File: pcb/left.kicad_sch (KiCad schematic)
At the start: 59 parts, among them J10 Conn_01x15_Pin, J11 Conn_ARM_SWD_TagConnect_TC203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, J12 Conn_01x02_Socket, J7 Conn_01x15_Pin, J8 USB_C_Receptacle_USB2.0_16P, J9 Conn_01x15_Pin, Q2 IRLML6402, SW19 SW_Push, SW21 SW_Push, SW22 MX_SW_HS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

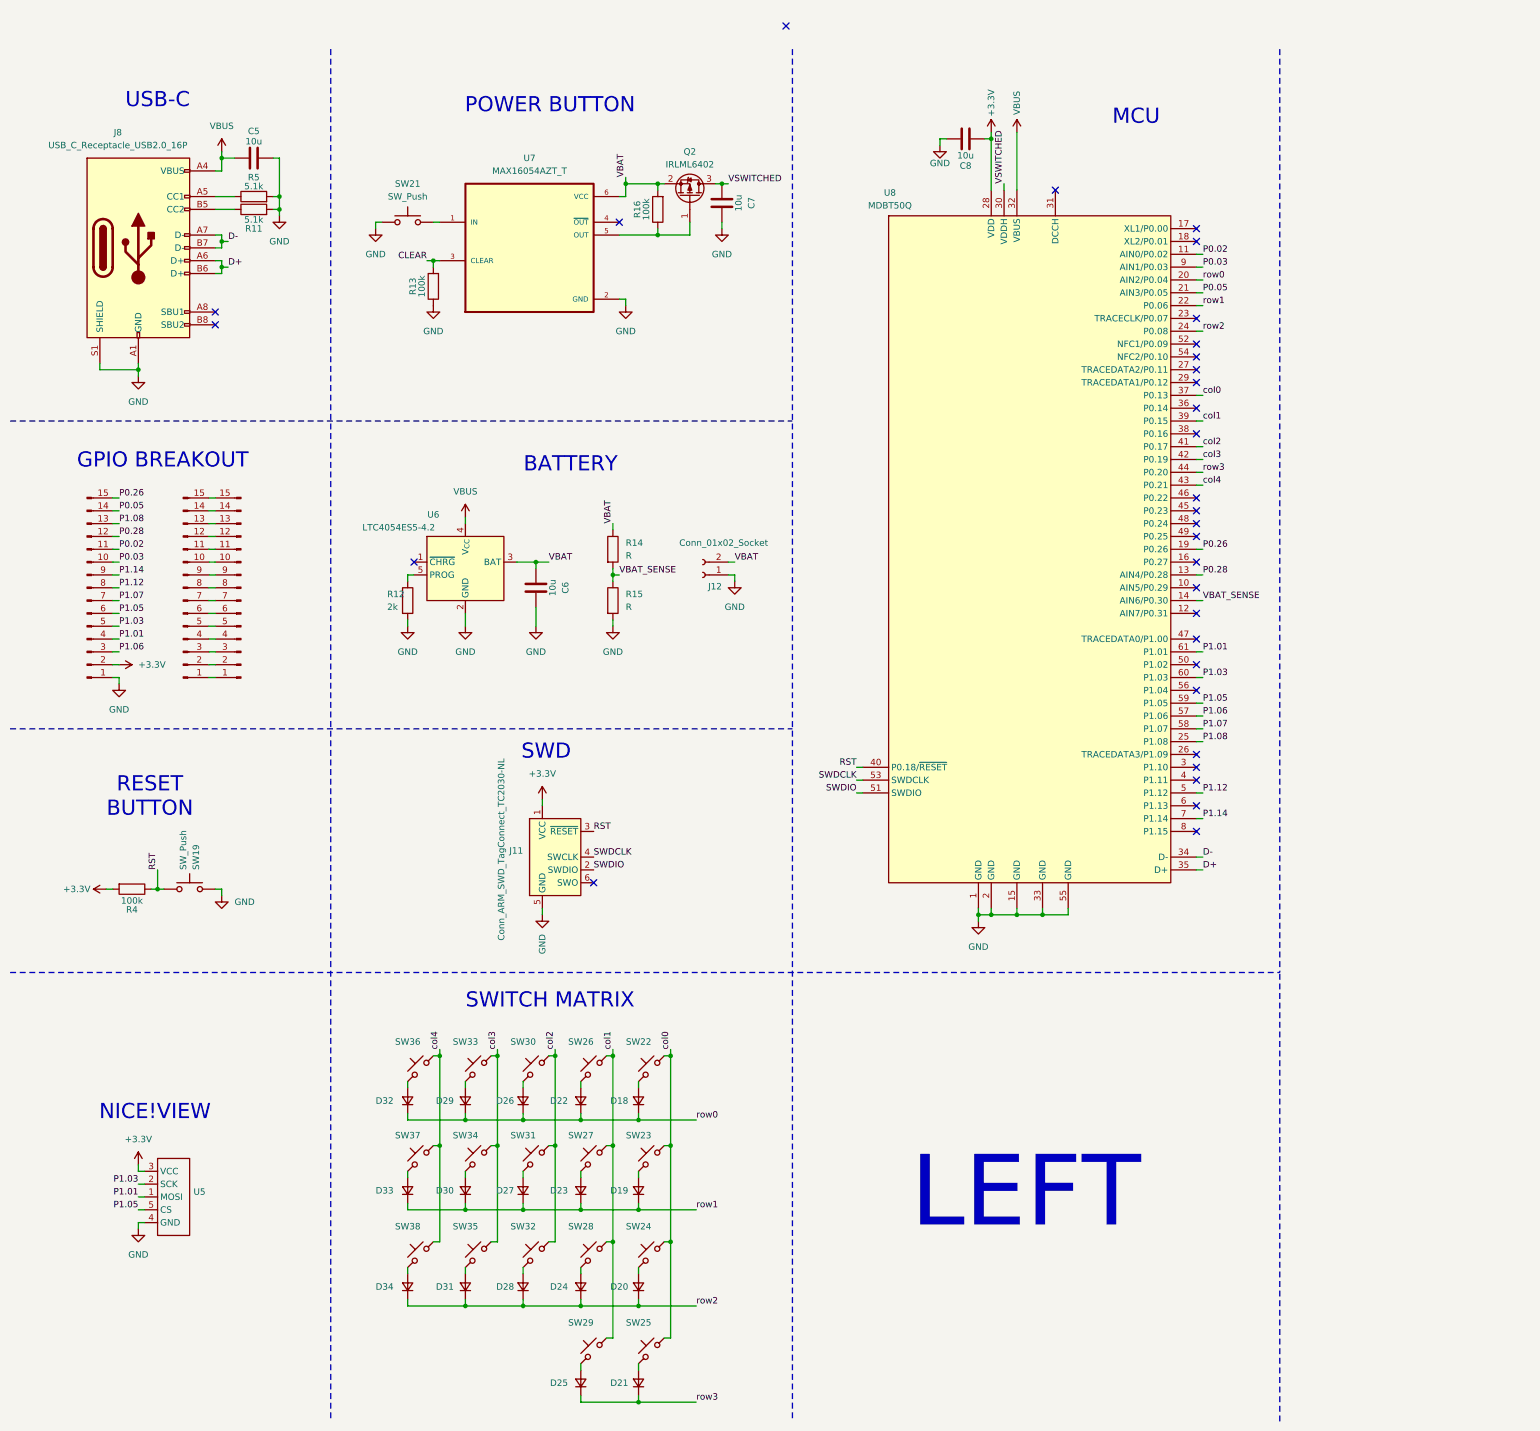
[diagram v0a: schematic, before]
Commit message: added ESD-protection
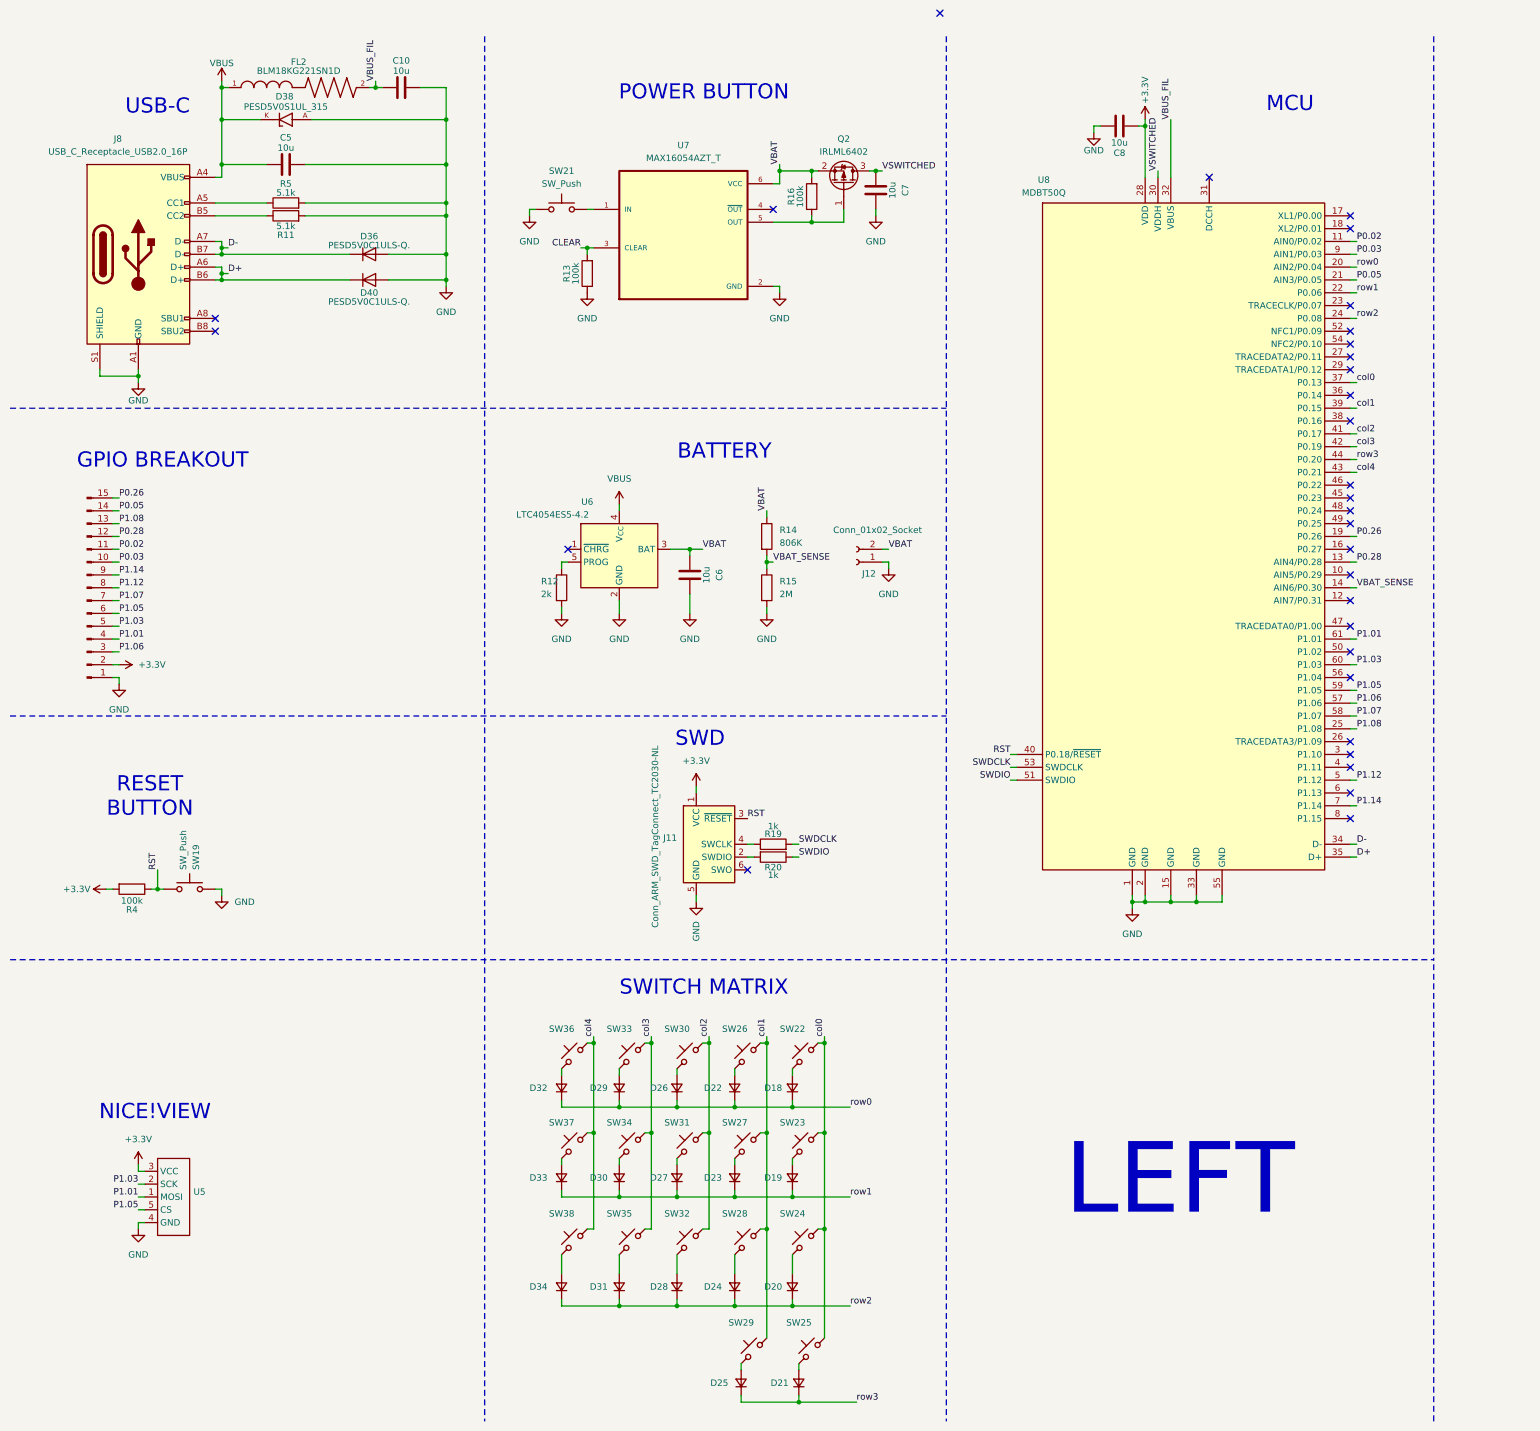
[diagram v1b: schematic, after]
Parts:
- removed J10: Conn_01x15_Pin, Connector_PinHeader_2.54mm:PinHeader_1x15_P2.54mm_Vertical, symbol Connector:Conn_01x15_Pin
- removed J9: Conn_01x15_Pin, Connector_FFC-FPC:Hirose_FH12-15S-0.5SH_1x15-1MP_P0.50mm_Horizontal, symbol Connector:Conn_01x15_Pin
- added C10: 10u, Capacitor_SMD:C_0603_1608Metric_Pad1.08x0.95mm_HandSolder, symbol Device:C
- added D36, D40: PESD5V0C1ULS-Q., Diode_SMD:D_SOD-882D, symbol Device:D
- added D38: PESD5V0S1UL_315, custom-libary:DIO_PESD5V0S1UL_315, symbol custom-libary:PESD5V0S1UL_315
- added FL2: BLM18KG221SN1D, custom-libary:BEADC1608X95N, symbol custom-libary:BLM18KG221SN1D
- added R19, R20: 1k, Resistor_SMD:R_0603_1608Metric_Pad0.98x0.95mm_HandSolder, symbol Device:R
- R14: value R -> 806K
- R15: value R -> 2M
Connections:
- net D+: now also D40.1 (K)
- net D-: now also D36.1 (K)
- net GND: now also C10.2, D36.2 (A), D38.A, D40.2 (A)
- net SWDCLK: now also R19.2; no longer J11.4 (SWCLK)
- net SWDIO: now also R20.1; no longer J11.2 (SWDIO)
- net VBUS: now also D38.K, FL2.1; no longer U8.32 (VBUS)
- new net: J11.2 (SWDIO), R20.2
- new net: J11.4 (SWCLK), R19.1
- new net VBUS_FIL: C10.1, FL2.2, U8.32 (VBUS)
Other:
- moved on the sheet: C5, C6, C7, C8, D18, D19, D20, D21, D22, D23, D24, D25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

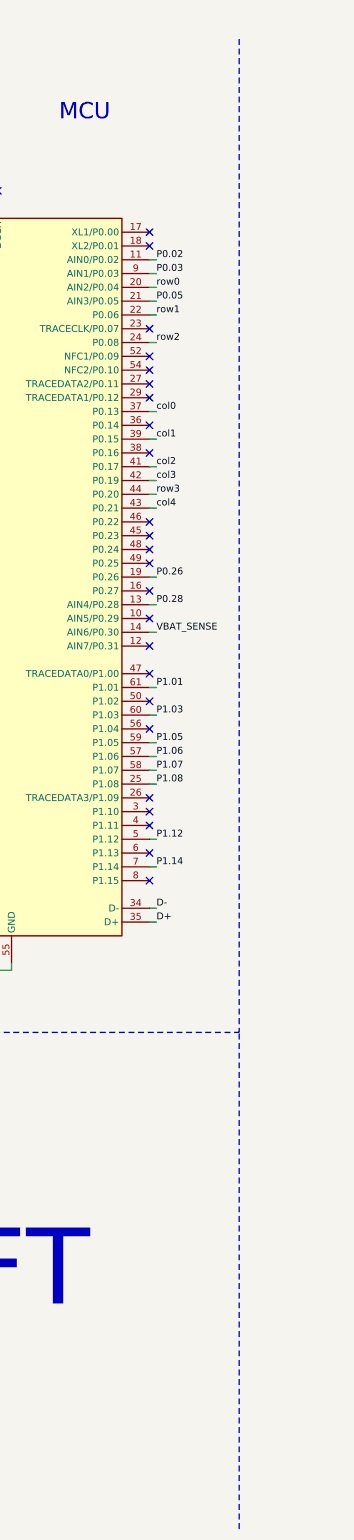
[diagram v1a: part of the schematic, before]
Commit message: added external oszilator
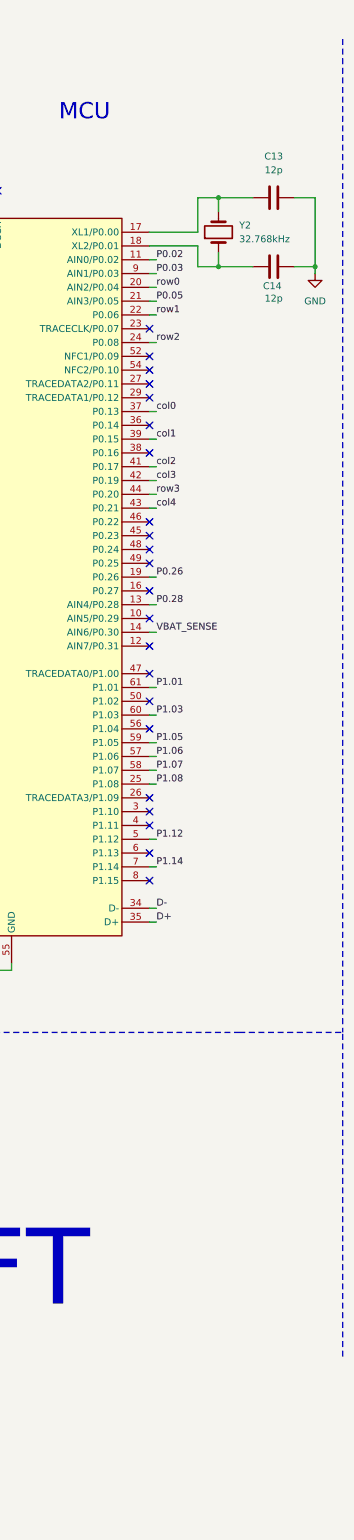
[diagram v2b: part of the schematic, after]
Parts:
- added C13, C14: 12p, Capacitor_SMD:C_0603_1608Metric_Pad1.08x0.95mm_HandSolder, symbol Device:C
- added Y2: 32.768kHz, custom-libary:FC2012SN32768K90NNA0KC0, symbol Device:Crystal
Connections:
- net GND: now also C13.1, C14.1
- net at U8.17 (XL1/P0.00): now also C13.2, Y2.2
- net at U8.18 (XL2/P0.01): now also C14.2, Y2.1
- no-connect marks 31 -> 29

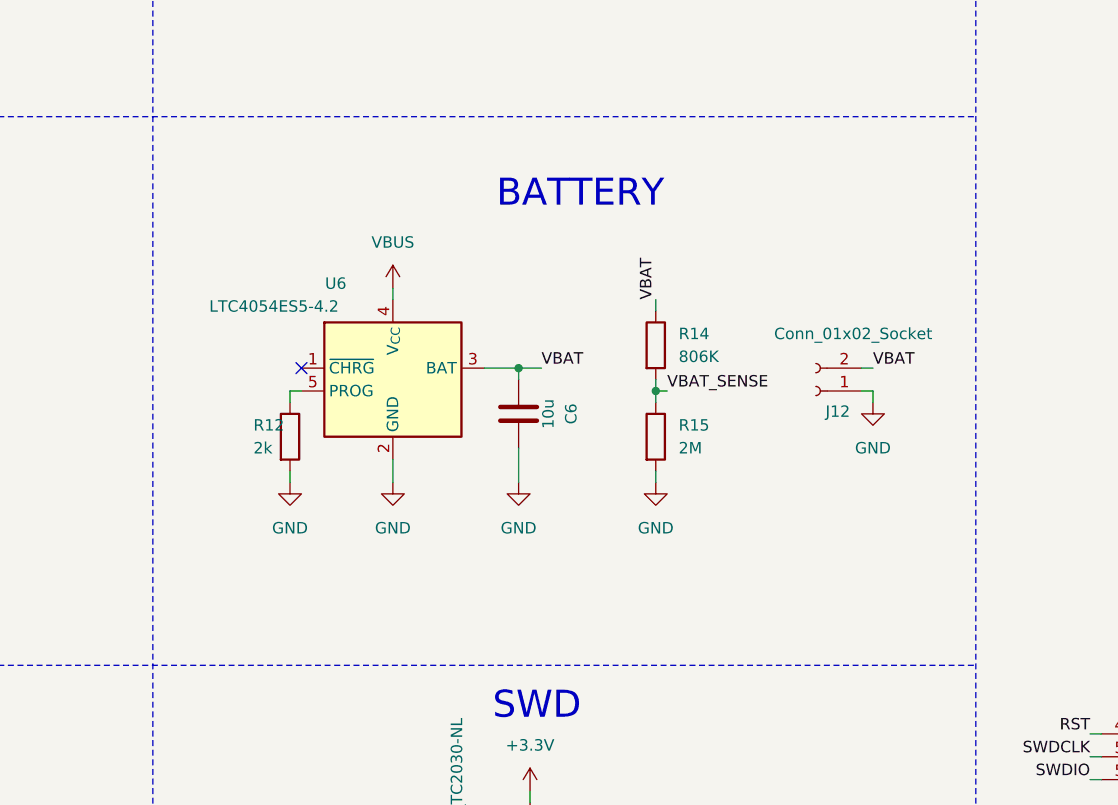
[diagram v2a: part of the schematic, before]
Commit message: replaced charge circuit for cost reasons
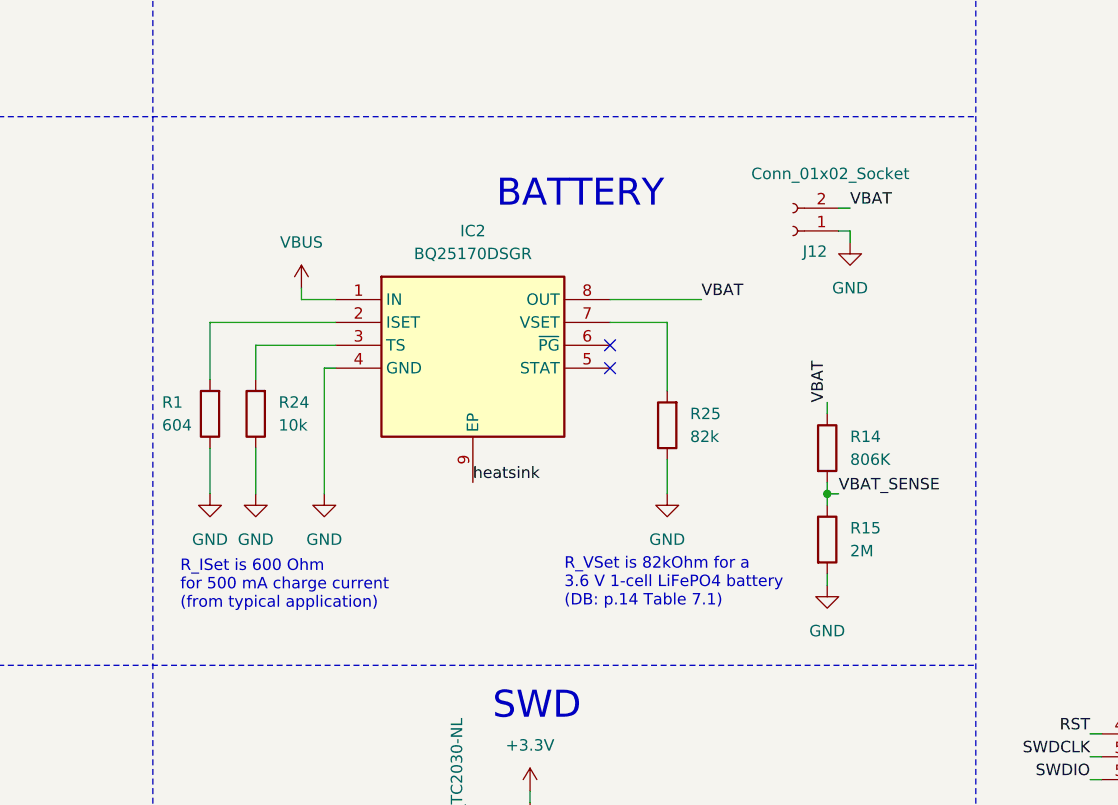
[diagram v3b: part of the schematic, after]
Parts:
- removed C6: 10u, Capacitor_SMD:C_0603_1608Metric_Pad1.08x0.95mm_HandSolder, symbol Device:C
- removed R12: 2k, Resistor_SMD:R_0603_1608Metric_Pad0.98x0.95mm_HandSolder, symbol Device:R
- removed U6: LTC4054ES5-4.2, Package_TO_SOT_SMD:TSOT-23-5, symbol Battery_Management:LTC4054ES5-4.2
- added IC2: BQ25170DSGR, SON50P200X200X80-9N, symbol BQ25170DSGR:BQ25170DSGR
- added R1: 604, Resistor_SMD:R_0603_1608Metric_Pad0.98x0.95mm_HandSolder, symbol Device:R
- added R24: 10k, Resistor_SMD:R_0603_1608Metric_Pad0.98x0.95mm_HandSolder, symbol Device:R
- added R25: 82k, Resistor_SMD:R_0603_1608Metric_Pad0.98x0.95mm_HandSolder, symbol Device:R
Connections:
- net GND: now also IC2.4 (GND), R1.1, R24.1, R25.1
- net VBAT: now also IC2.8 (OUT)
- net VBUS: now also IC2.1 (IN)
- new net: IC2.2 (ISET), R1.2
- new net: IC2.3 (TS), R24.2
- new net: IC2.7 (VSET), R25.2
- new net heatsink: IC2.9 (EP)
- no-connect marks 29 -> 30
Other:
- note added: "R_ISet is 600 Ohm for 500 mA charge current (from typical application)"
- note added: "R_VSet is 82kOhm for a 3.6 V 1-cell LiFePO4 battery (DB: p.14 Table 7.1)"
- moved on the sheet: J12, R14, R15

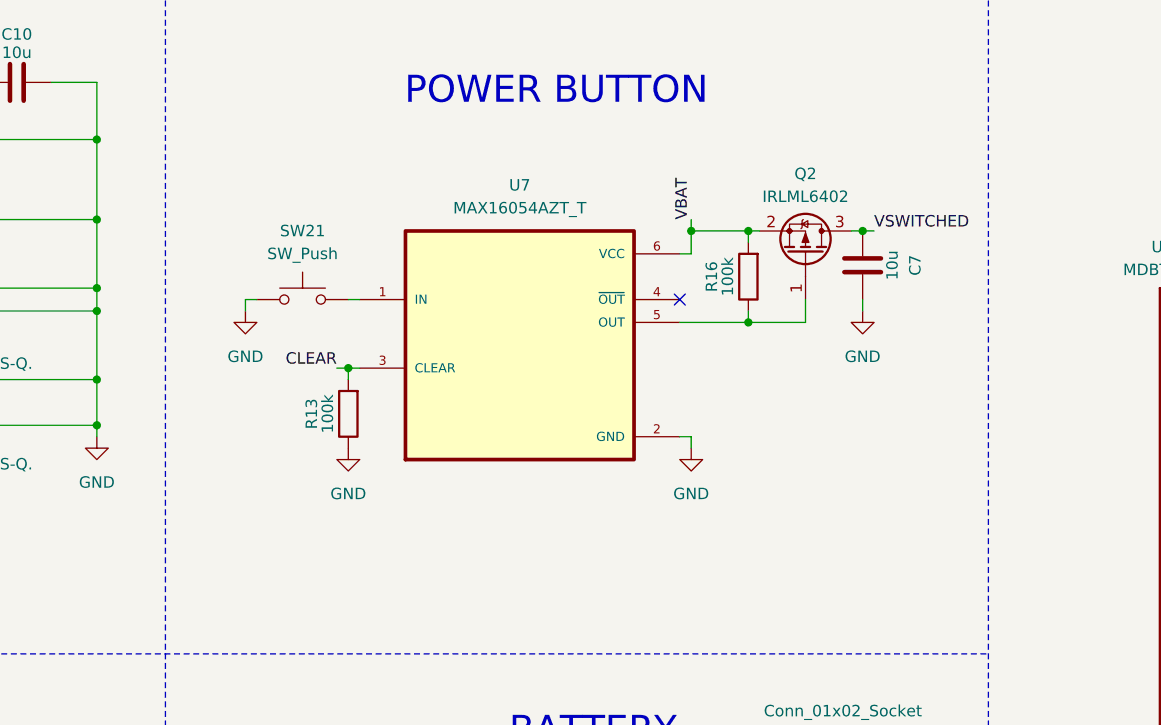
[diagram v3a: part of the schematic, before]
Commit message: replaced button ic and updated bom
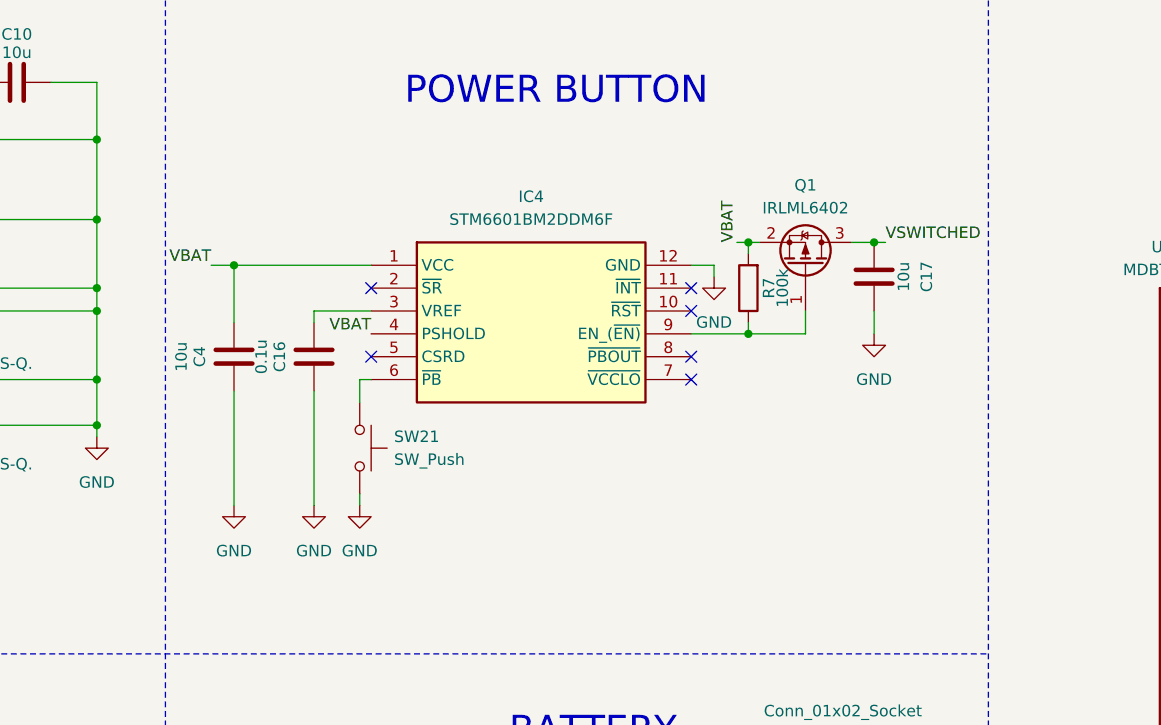
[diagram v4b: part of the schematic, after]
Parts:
- removed C7: 10u, Capacitor_SMD:C_0603_1608Metric_Pad1.08x0.95mm_HandSolder, symbol Device:C
- removed Q2: IRLML6402, Package_TO_SOT_SMD:SOT-23, symbol Transistor_FET:IRLML6402
- removed R13, R16: 100k, Resistor_SMD:R_0603_1608Metric_Pad0.98x0.95mm_HandSolder, symbol Device:R
- removed U7: MAX16054AZT_T, custom-libary:SOT95P275X110-6N, symbol custom-libary:MAX16054AZT_T
- added C16: 0.1u, Capacitor_SMD:C_0603_1608Metric_Pad1.08x0.95mm_HandSolder, symbol Device:C
- added C17, C4: 10u, Capacitor_SMD:C_0603_1608Metric_Pad1.08x0.95mm_HandSolder, symbol Device:C
- added IC4: STM6601BM2DDM6F, custom-libary:STM6601BM2DDM6F, symbol custom-libary:STM6601BM2DDM6F
- added Q1: IRLML6402, Package_TO_SOT_SMD:SOT-23, symbol Transistor_FET:IRLML6402
- added R7: 100k, Resistor_SMD:R_0603_1608Metric_Pad0.98x0.95mm_HandSolder, symbol Device:R
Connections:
- net GND: now also C16.2, C17.2, C4.2, IC4.12 (GND)
- net VBAT: now also C4.1, IC4.1 (VCC), IC4.4 (PSHOLD), Q1.2 (S), R7.2
- net VSWITCHED: now also C17.1, Q1.3 (D)
- net at SW21.1: now also IC4.6 (~{PB})
- new net: IC4.9 (EN_(~{EN)}), Q1.1 (G), R7.1
- new net: C16.1, IC4.3 (VREF)
- no-connect marks 30 -> 35
